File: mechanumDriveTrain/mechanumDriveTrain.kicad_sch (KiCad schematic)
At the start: 19 parts, among them IC1 TCAN3414DR, J1 XT30U-M, J2 BM02B-SRSS-TB, J3 Conn_01x08, J4 Conn_01x08, J5 Conn_01x08, J6 Conn_01x08, U1 Teensy 4.1, U2 LD1117S50TR_SOT223

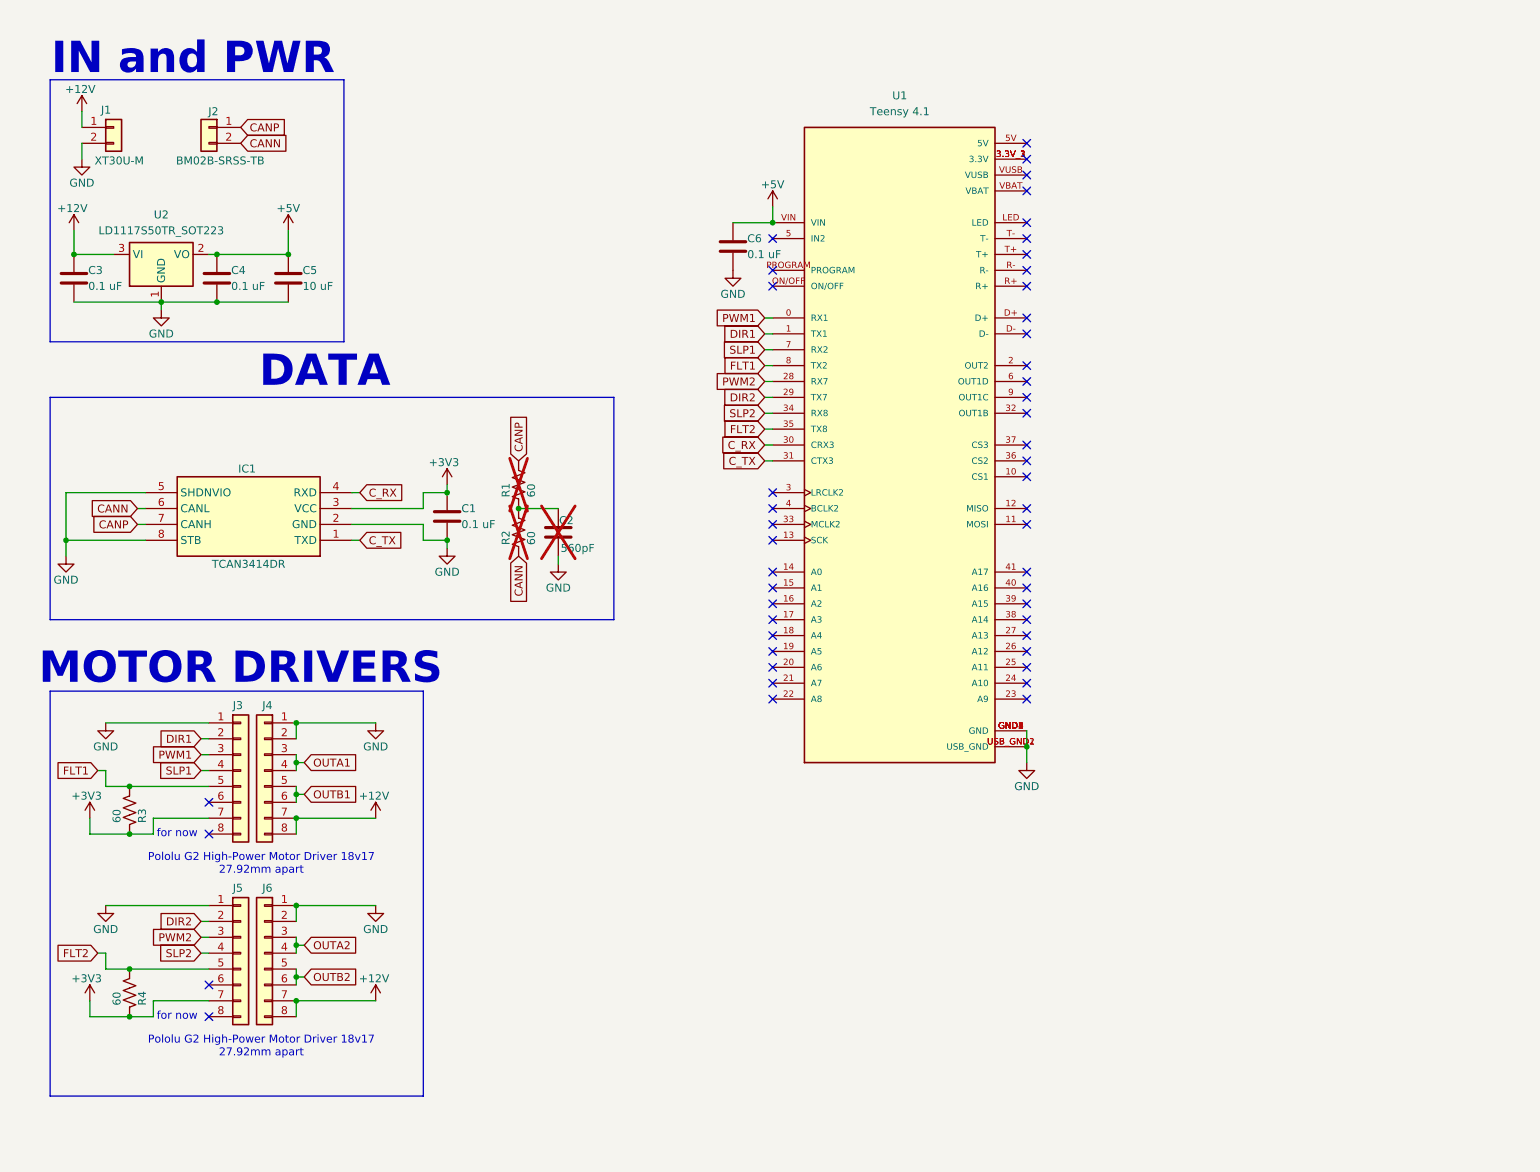
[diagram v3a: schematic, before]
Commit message: create symbol and footprint for the Pololu 18v17 motor controller
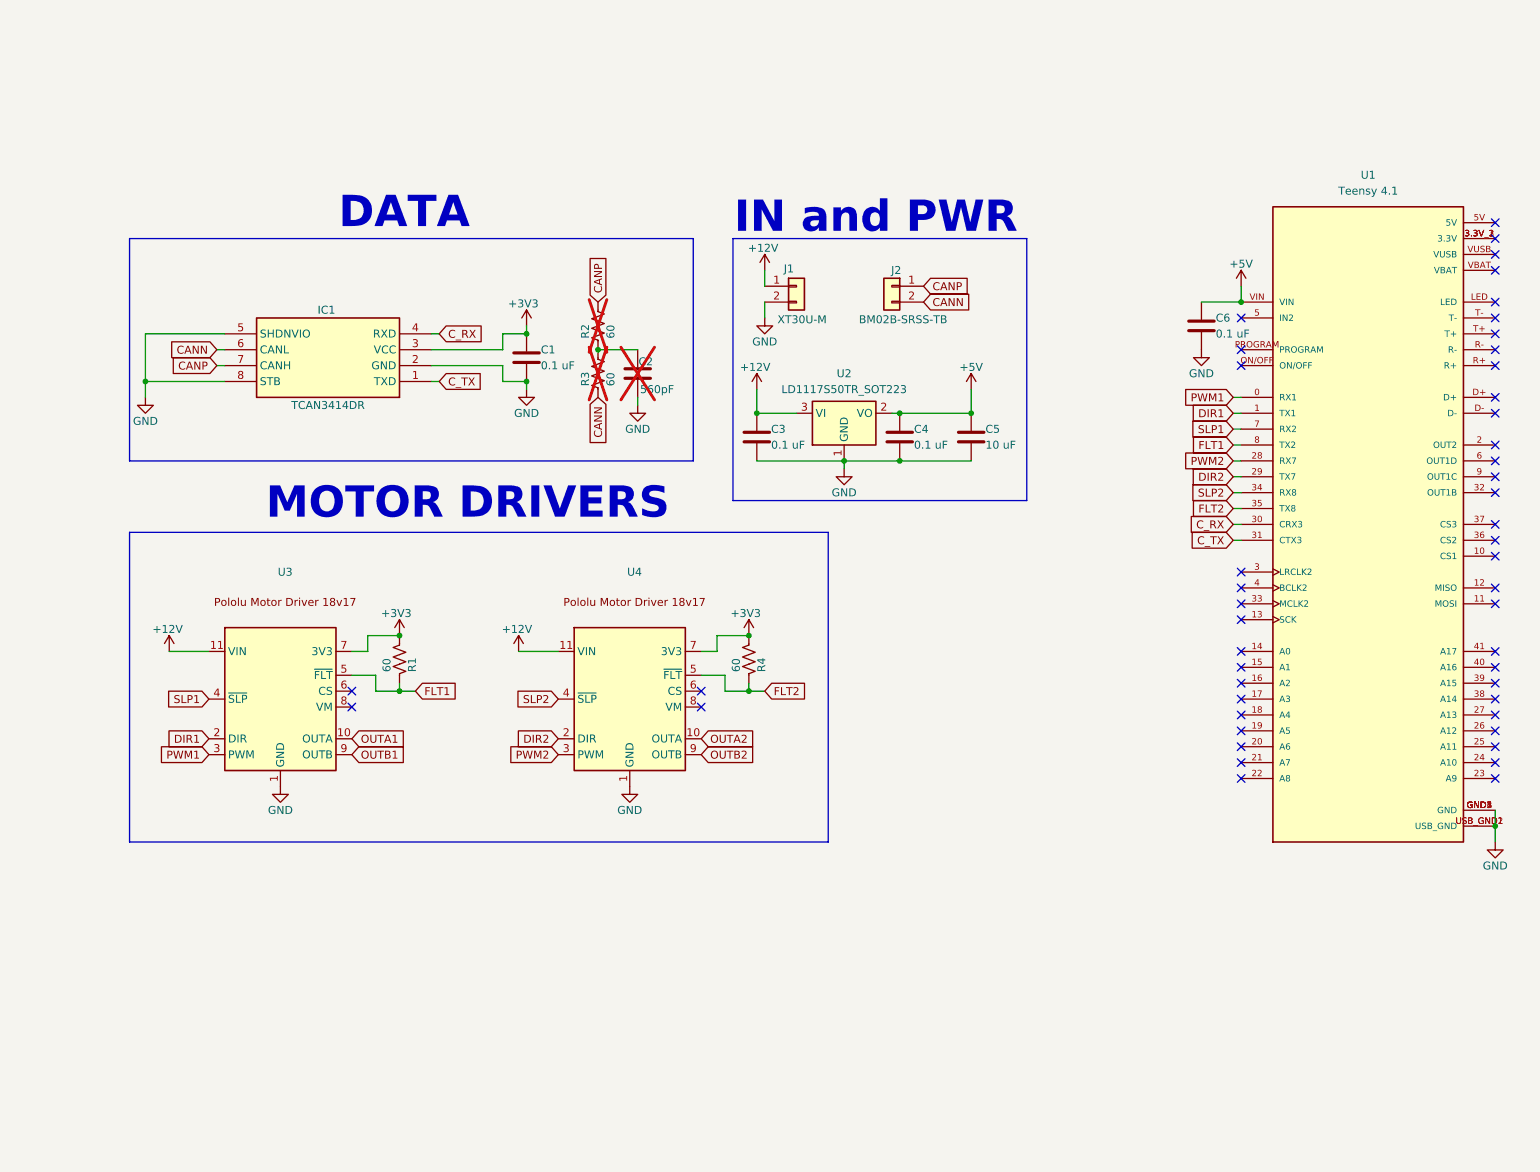
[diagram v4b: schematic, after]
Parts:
- removed J3, J4, J5, J6: Conn_01x08, Connector_PinSocket_2.54mm:PinSocket_1x08_P2.54mm_Vertical, symbol Connector_Generic:Conn_01x08
- removed R3: 60, Resistor_SMD:R_0805_2012Metric_Pad1.20x1.40mm_HandSolder, symbol Device:R_US
- added R1: 60, Resistor_SMD:R_0805_2012Metric_Pad1.20x1.40mm_HandSolder, symbol Device:R_US
- added U3, U4: ~, PolouMotorDriver:Pololu_G2_Motor_Driver_18v17, symbol PolouMotorDriver:Pololu_Motor_Driver_18v17
- IC1: footprint Package_SO:SOIC-8_3.9x4.9mm_P1.27mm -> SOIC127P600X175-8N
- U1: footprint Custom Footprints:Teensy41 -> DEV-16771:MODULE_DEV-16771
- renumbered R1 to R2, R2 to R3
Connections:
- net +12V: now also U3.11 (VIN), U4.11 (VIN)
- net +3V3: now also R4.1, R1.1, U3.7 (3V3), U4.7 (3V3); no longer R4.2
- net DIR1: now also U3.2 (DIR)
- net DIR2: now also U4.2 (DIR)
- net FLT1: now also R1.2, U3.5 (~{FLT})
- net FLT2: now also R4.2, U4.5 (~{FLT}); no longer R4.1
- net GND: now also U3.1 (GND), U4.1 (GND)
- net OUTA1: now also U3.10 (OUTA)
- net OUTA2: now also U4.10 (OUTA)
- net OUTB1: now also U3.9 (OUTB)
- net OUTB2: now also U4.9 (OUTB)
- net PWM1: now also U3.3 (PWM)
- net PWM2: now also U4.3 (PWM)
- net SLP1: now also U3.4 (~{SLP})
- net SLP2: now also U4.4 (~{SLP})
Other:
- note removed: "Pololu G2 High-Power Motor Driver 18v17 27.92mm apart"
- note removed: "for now"
- moved on the sheet: C1, C2, C3, C4, C5, C6, IC1, J1, J2, R2, R3, U1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

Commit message: Added connectors for motos, added schematic
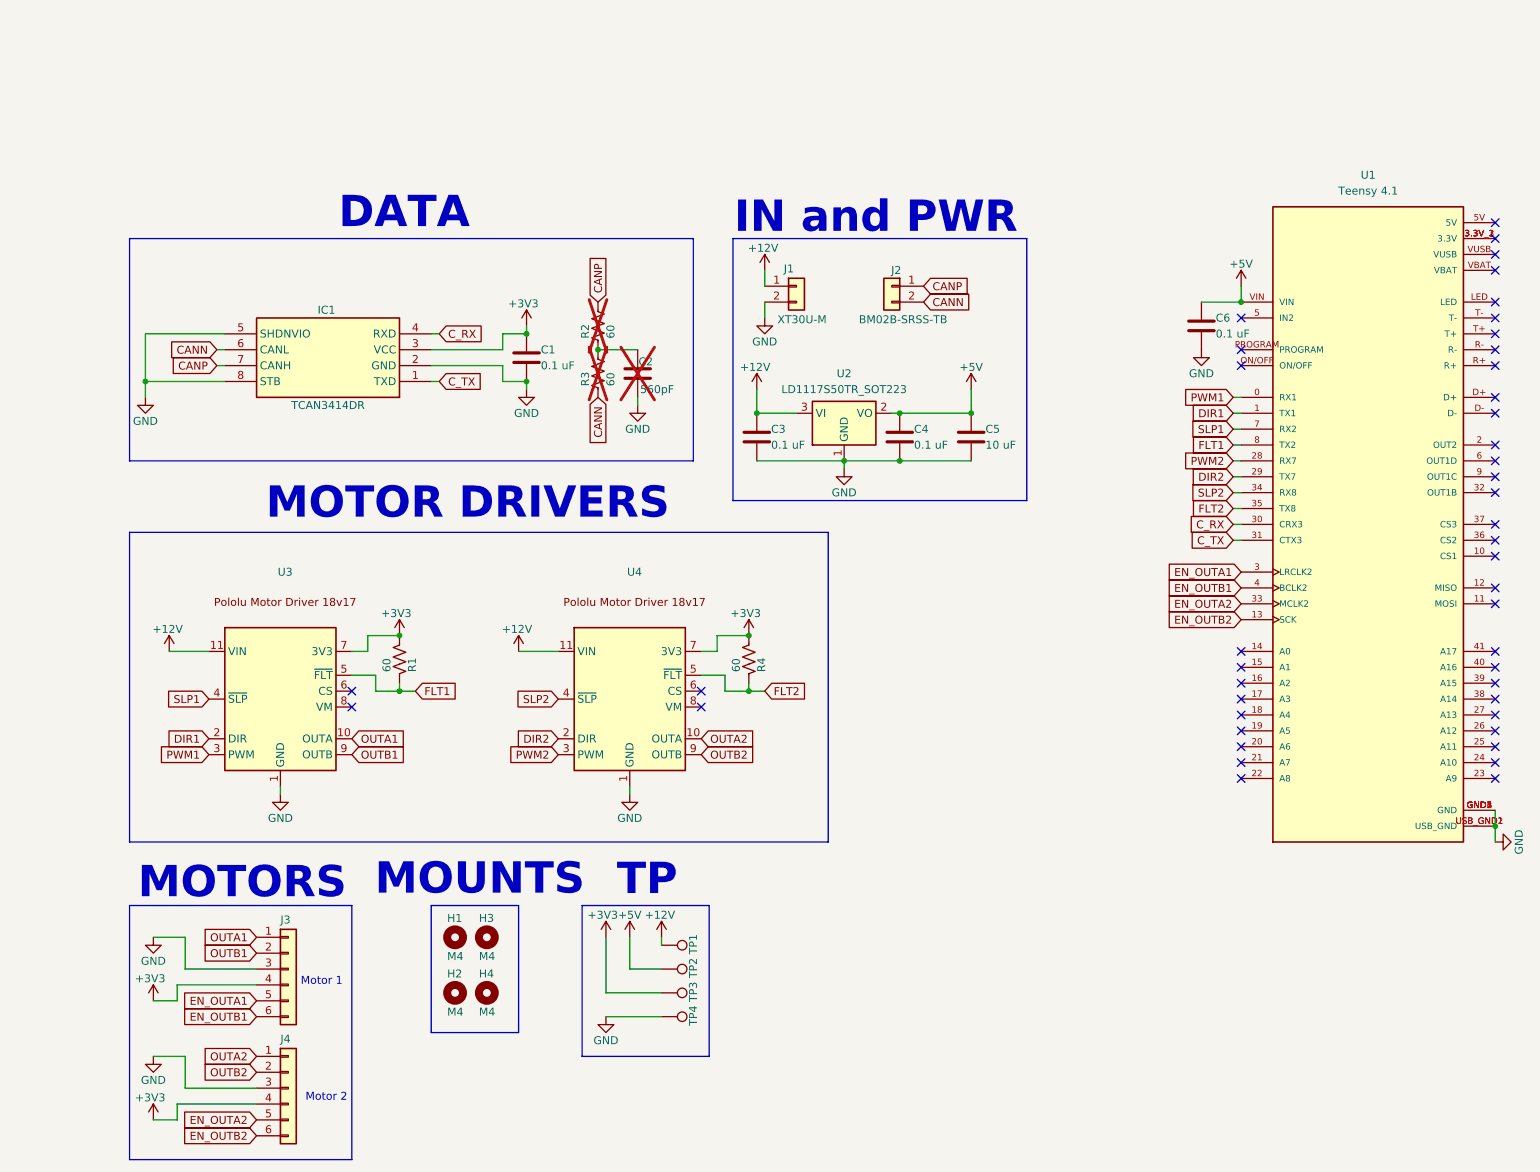
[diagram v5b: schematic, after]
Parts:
- added H1, H2, H3, H4: M4, MountingHole:MountingHole_4.3mm_M4_DIN965, symbol Mechanical:MountingHole
- added J3, J4: 5 pin dupont, Connector_PinHeader_2.54mm:PinHeader_1x06_P2.54mm_Vertical, symbol Connector_Generic:Conn_01x06
- added TP1, TP2, TP3, TP4: ~, TestPoint:TestPoint_Loop_D1.80mm_Drill1.0mm_Beaded, symbol Connector:TestPoint
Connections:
- net +12V: now also TP1.1
- net +3V3: now also J3.4 (Pin_4), J4.4 (Pin_4), TP3.1
- net +5V: now also TP2.1
- net GND: now also J3.3 (Pin_3), J4.3 (Pin_3), TP4.1
- net OUTA1: now also J3.1 (Pin_1)
- net OUTA2: now also J4.1 (Pin_1)
- net OUTB1: now also J3.2 (Pin_2)
- net OUTB2: now also J4.2 (Pin_2)
- net EN_OUTB2: now reaches U1.13 (SCK)
- net EN_OUTB2: now also J4.6 (Pin_6)
- net EN_OUTA1: now reaches U1.3 (LRCLK2)
- net EN_OUTA1: now also J3.5 (Pin_5)
- net EN_OUTA2: now reaches U1.33 (MCLK2)
- net EN_OUTA2: now also J4.5 (Pin_5)
- net EN_OUTB1: now reaches U1.4 (BCLK2)
- net EN_OUTB1: now also J3.6 (Pin_6)
- no-connect marks 49 -> 45
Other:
- note added: "MOTORS"
- note added: "MOUNTS"
- note added: "Motor 1"
- note added: "Motor 2"
- note added: "TP"

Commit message: Updated schematic, started new layout of board
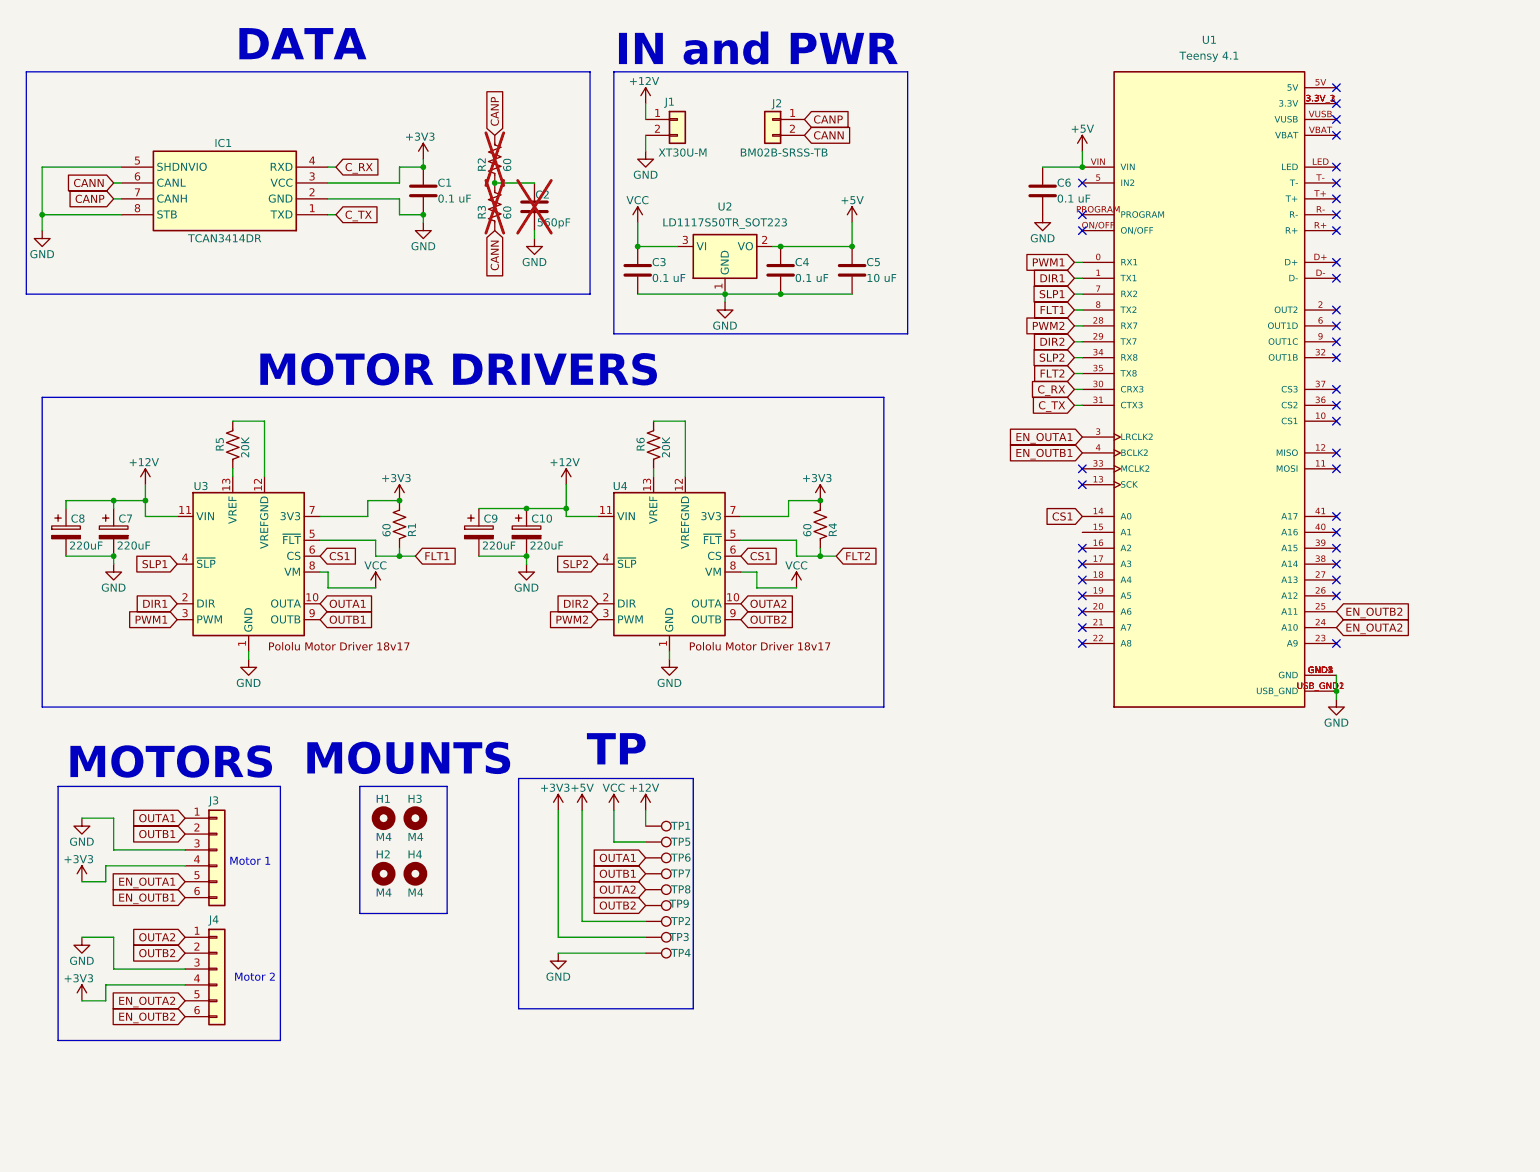
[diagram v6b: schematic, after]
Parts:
- added C10, C7, C8, C9: 220uF, Capacitor_THT:CP_Radial_D6.3mm_P2.50mm, symbol Device:C_Polarized
- added R5, R6: 20K, Resistor_SMD:R_0805_2012Metric_Pad1.20x1.40mm_HandSolder, symbol Device:R_US
- added TP5, TP6, TP7, TP8, TP9: ~, TestPoint:TestPoint_Loop_D1.80mm_Drill1.0mm_Beaded, symbol Connector:TestPoint
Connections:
- net +12V: now also C10.1, C7.1, C8.1, C9.1; no longer C3.1, U2.3 (VI)
- net EN_OUTA2: now also U1.24 (A10); no longer U1.33 (MCLK2)
- net EN_OUTB2: now also U1.25 (A11); no longer U1.13 (SCK)
- net GND: now also C10.2, C7.2, C8.2, C9.2
- net OUTA1: now also TP6.1
- net OUTA2: now also TP8.1
- net OUTB1: now also TP7.1
- net OUTB2: now also TP9.1
- net CS1: now reaches U4.6 (CS)
- net CS1: now also U1.14 (A0), U3.6 (CS)
- net VCC: now reaches U4.8 (VM)
- net VCC: now also C3.1, U2.3 (VI), U3.8 (VM), TP5.1
- new net: R6.1, U4.13 (VREF)
- new net: R6.2, U4.12 (VREFGND)
- new net: R5.1, U3.13 (VREF)
- new net: R5.2, U3.12 (VREFGND)
- no-connect marks 45 -> 39
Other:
- moved on the sheet: C1, C2, C3, C4, C5, C6, H1, H2, H3, H4, IC1, J1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

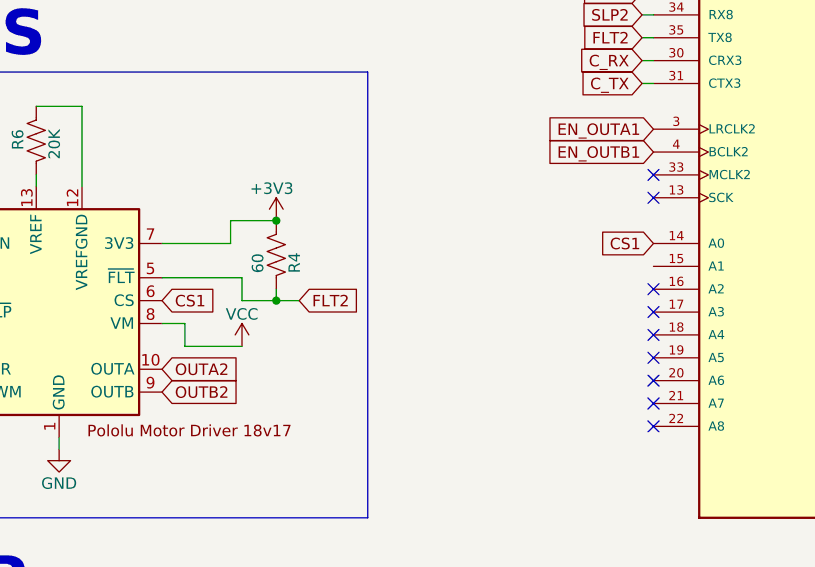
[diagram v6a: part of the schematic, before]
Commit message: Added cs2
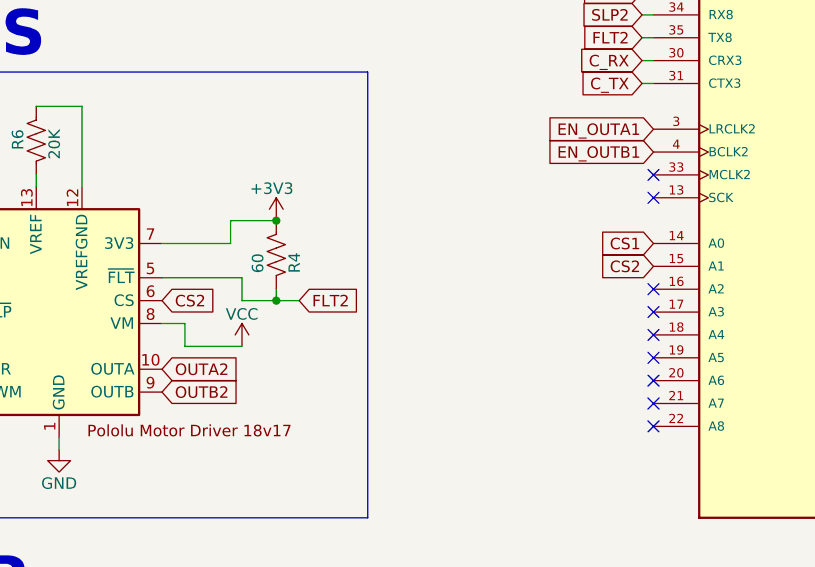
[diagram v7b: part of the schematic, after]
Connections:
- net CS1: no longer U4.6 (CS)
- net CS2: now reaches U1.15 (A1)
- net CS2: now also U4.6 (CS)
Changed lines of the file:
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@@
+		)
+	)
+	(global_label "CS2"
+		(shape input)
+		(at 184.15 95.25 180)
+		(fields_autoplaced yes)
+		(effects
+			(font
+				(size 1.27 1.27)
+			)
+			(justify right)
+		)
+		(property "Intersheetrefs" "${INTERSHEET_REFS}"
+			(at 177.4758 95.25 0)
+			(effects
+				(font
+					(size 1.27 1.27)
+				)
+				(justify right)
+				(hide yes)
+			)
 		)
 	)
@@
 		)
 	)
-	(global_label "CS1"
+	(global_label "CS2"
 		(shape input)
 		(at 129.54 99.06 0)
